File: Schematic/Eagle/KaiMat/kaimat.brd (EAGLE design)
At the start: 60.1 x 110.5 mm, 22 parts, among them U1 THONKICONNNEW, U10 THONKICONNNEW, U11 THONKICONNNEW, U12 THONKICONNNEW, U2 THONKICONNNEW, U3 THONKICONNNEW, U4 THONKICONNNEW, U5 THONKICONNNEW, U6 THONKICONNNEW, U7 THONKICONNNEW, U8 THONKICONNNEW, U9 THONKICONNNEW

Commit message: pcb and eagle sch
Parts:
- moved ENC1 0.50 mm to (35.7, 75.7)
- moved ENC2 0.50 mm to (51.3, 75.7)
- moved S1 0.50 mm to (35.7, 63.5)
- moved S2 0.50 mm to (51.3, 63.5)
- moved U$1 0.50 mm to (18.3, 30.9)
- moved U$3 0.50 mm to (13.1, 74.5)
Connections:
- removed net VCC: U$3.2
- net +5V: now also U$3.2
- net OLEDCLK: now also U$3.3
- net OLEDCS: now also U$3.7
- net OLEDDATA: now also U$3.4
- net OLEDDC: now also U$3.6
- net OLEDRST: now also U$3.5
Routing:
- net +5V: track 6.69 -> 7.19 mm

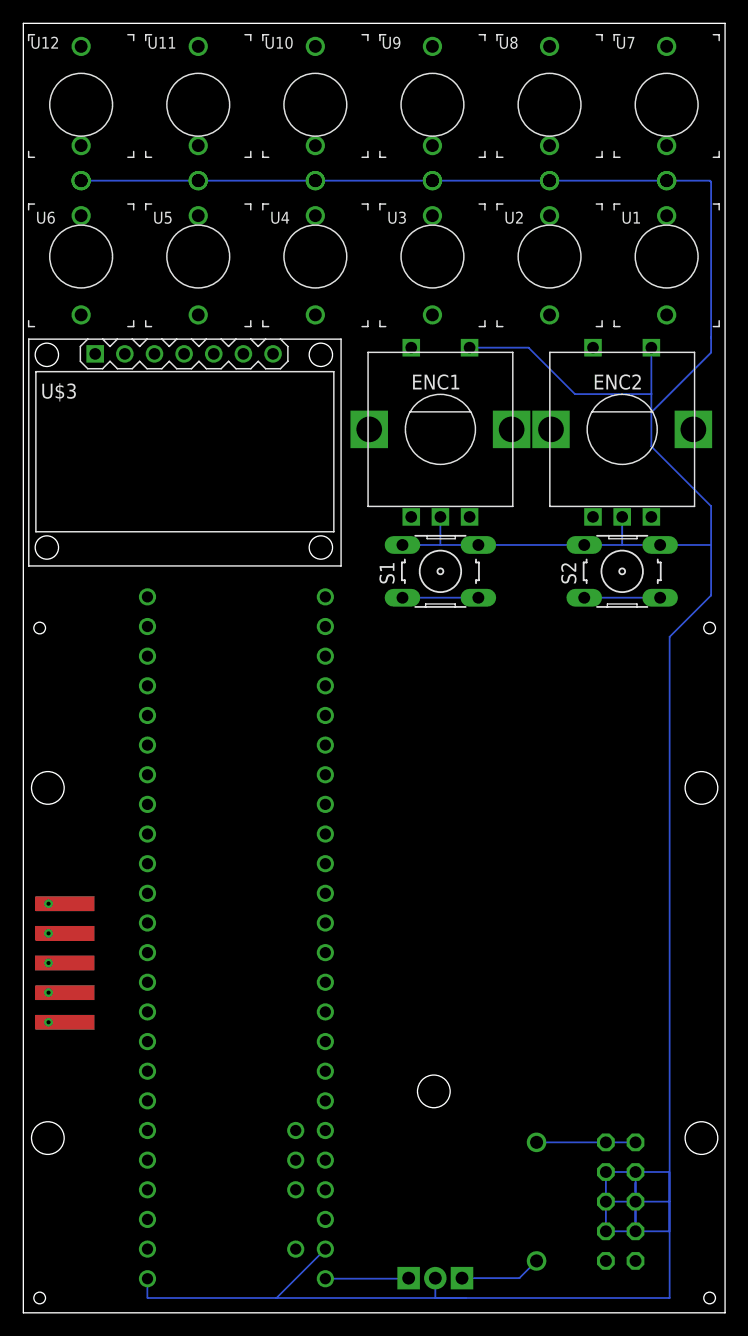
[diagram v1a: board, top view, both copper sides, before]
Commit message: changed to 128x64 OLED, improved schematic and code (latency)
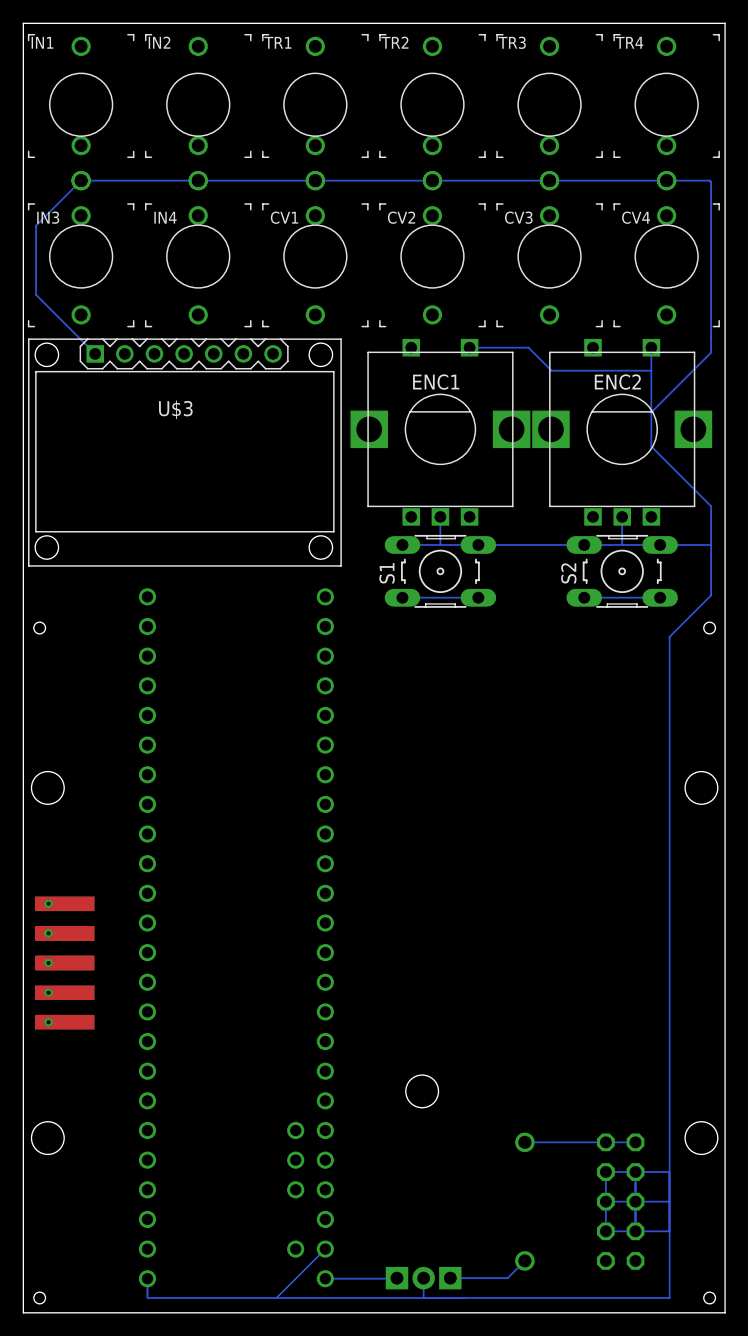
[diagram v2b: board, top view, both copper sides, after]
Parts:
- moved D1 1.00 mm to (43.0, 9.53)
- moved U$2 1.00 mm to (34.4, 12.6)
- renumbered U1 to CV4, U10 to TR1, U11 to IN2, U12 to IN1, U2 to CV3, U3 to CV2, U4 to CV1, U5 to IN4, U6 to IN3, U7 to TR4, U8 to TR3, U9 to TR2
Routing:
- net GND: track 302.6 -> 321.3 mm
- net N$1: track 8.48 -> 9.48 mm
- net +5V: track 7.19 -> 6.19 mm
